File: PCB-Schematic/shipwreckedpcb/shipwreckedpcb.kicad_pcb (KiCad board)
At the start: 4 copper layers, 61.8 x 79.6 mm, 182 parts, among them J1 USB4105, J14 Conn_01x01, J15 Conn_01x01, J16 Conn_01x01, J17 Conn_01x01, J18 Conn_01x01, J19 Conn_01x01, J2 Waveshare 1.54" E-Ink, J20 Conn_01x01, J21 Conn_01x01, J22 Conn_01x01, J23 Conn_01x01, J24 Conn_01x01, J25 Conn_01x01, J26 Conn_01x01, J28 Conn_01x01, J29 Conn_01x01, J3 Conn_01x01, J30 Conn_01x01, J31 Conn_01x01, J32 Conn_01x01, J33 Conn_01x01, J34 Conn_01x01, J35 Conn_01x01, J36 Conn_01x01, J37 Conn_01x01, J38 Conn_01x01, J39 Conn_01x01, J4 Conn_01x01, J40 Conn_01x01, J5 SWD, J6 Conn_01x01, J7 Conn_01x01, J8 B2B Male, J9 B2B Female, Q1 Si1308EDL, SW1 BOOTSEL, SW10 Resistive, SW11 Clicky - THT, SW12 Clicky - SMD, SW13 Clicky - THT, SW14 Clicky - SMD, SW15 Clicky - THT, SW16 Clicky - SMD, SW17 Clicky - THT, SW18 Clicky - SMD, SW19 PWR Switch, SW2 RESET, SW3 Resistive, SW4 Resistive, SW5 Resistive, SW6 Resistive, SW7 Resistive, SW8 Resistive, SW9 Resistive, U1 RP2040, U2 W25Q128JVS, U3 Si4463, U4 TPS61200DRC, U5 AS179-92LF, U6 AMS1117-3.3, U7 PCA9555PW, Y1 ABM8-272-T3, Y2 X322530MOB4SI

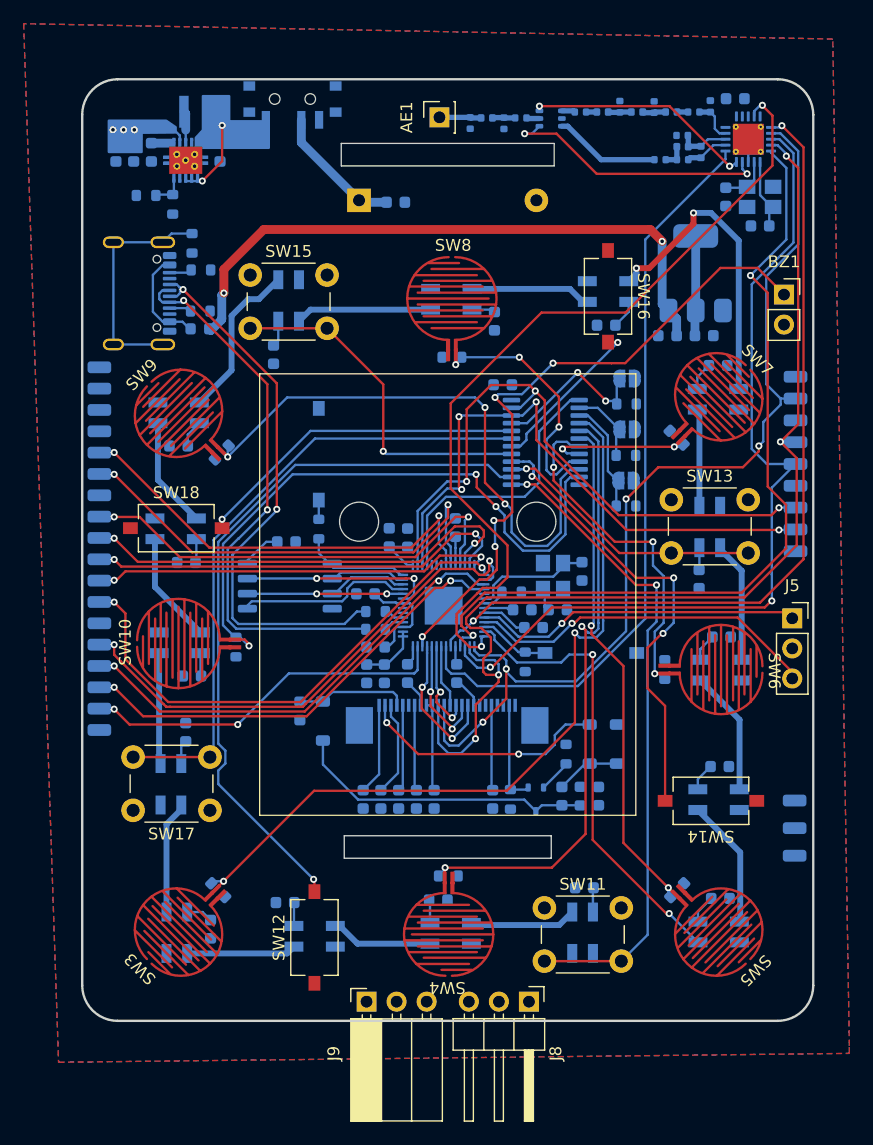
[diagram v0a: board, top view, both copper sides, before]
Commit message: fixed drc errors, added stitching vias
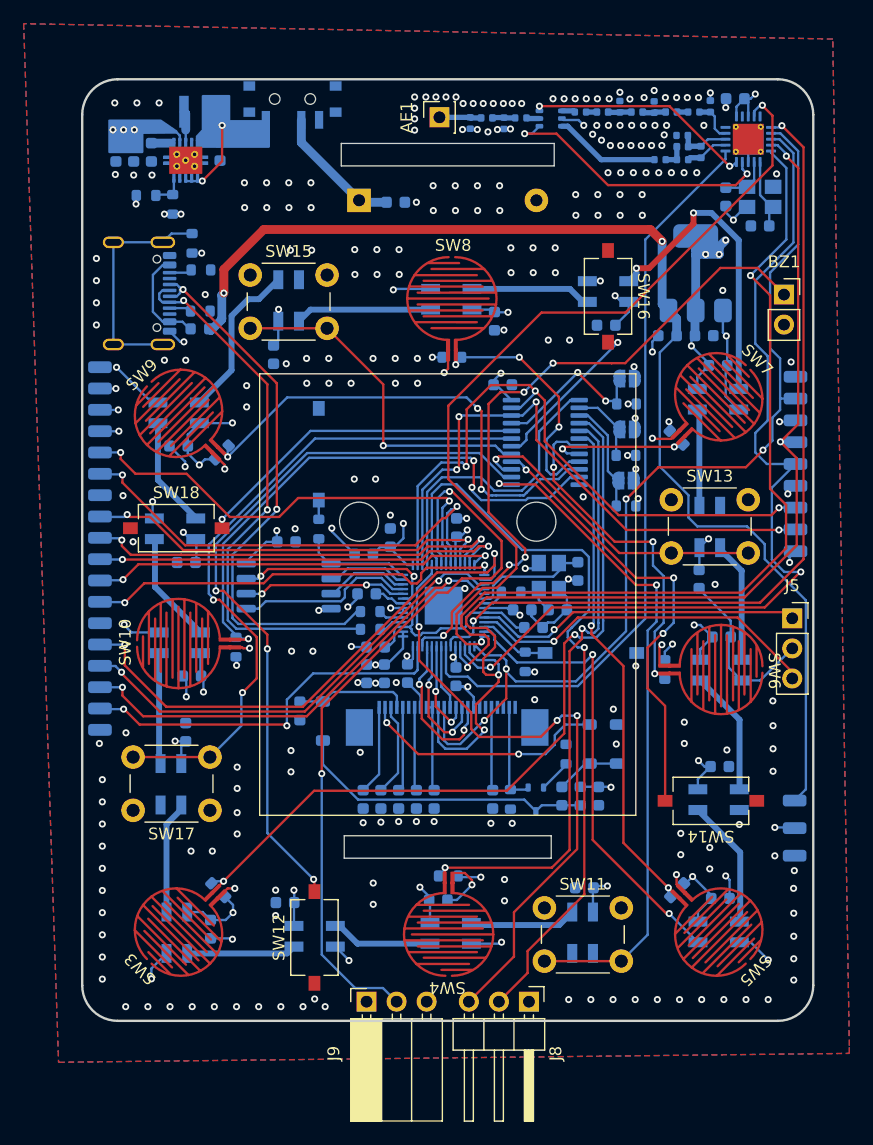
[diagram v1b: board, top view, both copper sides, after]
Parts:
- moved C5 3.96 mm to (139.9, 102.3), turned to 180 degrees
- moved R2 0.45 mm to (140.5, 107.2)
- moved R3 0.45 mm to (140.5, 108.7)
- moved C13 0.35 mm to (158.1, 103.8)
- moved Y1 0.35 mm to (155.6, 104.2)
- moved C8 0.27 mm to (147.8, 112.7)
- moved J2 0.17 mm to (147.0, 116.6)
- moved C6 0.10 mm to (147.8, 100.0)
- moved C1 0.10 mm to (140.2, 105.7)
- moved U2 0.10 mm to (133.6, 105.0)
- moved C4 0.09 mm to (142.2, 100.9)
- moved C53 0.08 mm to (127.8, 68.2)
- moved J24 0.05 mm to (117.7, 111.7)
- moved J6 0.05 mm to (117.7, 90.1)
- moved J14 0.05 mm to (117.7, 93.7)
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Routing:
- net Earth: track 6.95 -> 118.3 mm, vias 0 -> 266
- net +3V3: track 66.2 -> 141.7 mm, vias 3 -> 49
- net /B2B_TX: track 0.00 -> 64.6 mm, vias 0 -> 1
- net /B2B_RX: track 0.00 -> 64.4 mm, vias 0 -> 2
- net /B2B_DCT: track 0.00 -> 54.3 mm, vias 0 -> 3
- net +5V: track 53.1 -> 101.0 mm
- net /GPIO12: track 43.9 -> 35.7 mm
- net +1V1: track 12.8 -> 20.6 mm
- net /BUTT_7: track 49.4 -> 42.2 mm
- net /BUTT_8: track 53.6 -> 48.2 mm
- net /SI_NSEL: track 70.4 -> 75.3 mm
- net /BUTT_15: track 53.7 -> 57.4 mm, vias 0 -> 2
- net /BUTT_11: track 23.0 -> 26.6 mm
- net /SPI_MISO: track 75.0 -> 78.4 mm
- net /GPIO8: track 38.4 -> 35.3 mm
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
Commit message: started sx1262
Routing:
- net Earth: vias 266 -> 268
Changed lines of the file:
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@@
+	)
+	(via
+		(at 143.326388 90.45)
+		(size 0.6)
+		(drill 0.3)
+		(layers "F.Cu" "B.Cu")
+		(free yes)
+		(net 3)
 	)
 	(via
@@
 		(size 0.6)
 		(drill 0.3)
+		(layers "F.Cu" "B.Cu")
+		(free yes)
+		(net 3)
+	)
+	(via
+		(at 145.2 90.45)
+		(size 0.6)
+		(drill 0.3)

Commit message: finished prototype?
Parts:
- removed C26, C27, C28, C29, C30, C31, C32, C33, C34, C35, C36, C37, C38, C39, C40: 100nF, Capacitor_SMD:C_0603_1608Metric
- removed C41: 3.9pF, Capacitor_SMD:C_0402_1005Metric
- removed C42: 5.6pF, Capacitor_SMD:C_0402_1005Metric
- removed C43: 2.7pF, Capacitor_SMD:C_0402_1005Metric
- removed C44, C45, C48: 100pF, Capacitor_SMD:C_0402_1005Metric
- removed C46, C47: 4.3pF, Capacitor_SMD:C_0402_1005Metric
- removed C49: 1pF, Capacitor_SMD:C_0402_1005Metric
- removed C50: 3pF, Capacitor_SMD:C_0402_1005Metric
- removed C58, C59: 12pF, Capacitor_SMD:C_0603_1608Metric
- removed D21, D22, D23, D24, D25, D26, D27, D28, D29, D30, D31, D32, D33, D34, D35, D36: SK6812MINI, LED_SMD:LED_SK6812MINI_PLCC4_3.5x3.5mm_P1.75mm
- removed L2: 100nH, Inductor_SMD:L_0402_1005Metric
- removed L3: 12nH, Inductor_SMD:L_0402_1005Metric
- removed L4, L5: 10nH, Inductor_SMD:L_0402_1005Metric
- removed L6: 8.2nH, Inductor_SMD:L_0402_1005Metric
- removed L7: 22nH, Inductor_SMD:L_0402_1005Metric
- removed L8: 18nH, Inductor_SMD:L_0402_1005Metric
- removed U5: AS179-92LF, Package_TO_SOT_SMD:SOT-363_SC-70-6
- added C57: 47nF, Capacitor_SMD:C_0603_1608Metric, B.Cu at (167.8, 64.8)
- added C62: 47pF, Capacitor_SMD:C_0603_1608Metric, B.Cu at (166.3, 64.3)
- added C63: 100pF, Capacitor_SMD:C_0603_1608Metric, B.Cu at (155.2, 65.5)
- added C64: 1nF, Capacitor_SMD:C_0603_1608Metric, B.Cu at (158.3, 67.9)
- added C65: 100nF, Capacitor_SMD:C_0603_1608Metric, B.Cu at (169.3, 64.5)
- added C66: 100nF, Capacitor_SMD:C_0603_1608Metric, B.Cu at (175.1, 70.5)
- added C67: 470nF, Capacitor_SMD:C_0603_1608Metric, B.Cu at (175.2, 67.0)
- added D5: LED, LED_THT:LED_D5.0mm, B.Cu at (148.3, 65.0)
- added FL1: 0900FM15K0039, RF_Converter:Balun_Johanson_0900FM15K0039, B.Cu at (161.3, 65.2)
- added L10: 47nH, Inductor_SMD:L_0603_1608Metric, B.Cu at (164.1, 64.5)
- added L11: 15uH, Inductor_SMD:L_0805_2012Metric, B.Cu at (176.8, 67.3)
- added R23: 100, Resistor_SMD:R_0603_1608Metric, B.Cu at (161.3, 67.9)
- added U8: SX1262IMLTRT, Package_DFN_QFN:QFN-24-1EP_4x4mm_P0.5mm_EP2.6x2.6mm, B.Cu at (171.7, 68.6)
- C24, C25: value 100nF -> 8pF
- D1: footprint Diode_SMD:D_0603_1608Metric -> Diode_SMD:D_SOD-123F
- U3: value Si4463 -> PE4259; footprint Package_DFN_QFN:QFN-20-1EP_4x4mm_P0.5mm_EP2.6x2.6mm_ThermalVias -> Package_TO_SOT_SMD:SOT-363_SC-70-6
- Y2: value X322530MOB4SI -> 32MHz
- moved C25 67.5 mm to (175.1, 64.0), turned to -90 degrees
- moved U3 14.2 mm to (158.4, 65.5), turned to 180 degrees
- moved Y2 8.09 mm to (172.2, 64.1)
- moved C24 8.03 mm to (167.3, 70.8), turned to 90 degrees
- moved AE1 5.73 mm to (152.1, 64.8)
- moved D1 0.85 mm to (126.8, 83.7)
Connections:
- C24 pad 1: +3V3 -> Earth
- C24 pad 2: Earth -> /SX_XTA
- C25 pad 1: +3V3 -> Earth
- C25 pad 2: Earth -> /SX_XTB
- U1 pad 28: /SI_IO1 -> /SX_DIO1
- U1 pad 32: /SI_NSEL -> /SX_NSS
- U1 pad 34: /SI_NIRQ -> /SX_BUSY
- U1 pad 35: /SI_SDN -> /SX_NRST
- U3 pad 1: /SI_SDN -> Net-(FL1-SW_RFO)
- U3 pad 2: /SI_RXp -> Earth
- U3 pad 3: /SI_RXn -> Net-(FL1-SW_RFI)
- U3 pad 4: /SI_TX -> Net-(U3-CTRL)
- U3 pad 5: unconnected-(U3-NC-Pad5) -> Net-(U3-RFIN)
- Y2 pad 1: /SI_XOUT -> /SX_XTB
- Y2 pad 3: /SI_XIN -> /SX_XTA
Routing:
- net /SI_NSEL: track 75.3 -> 0.00 mm, vias 2 -> 0
- net /SX_NSS: track 0.00 -> 74.2 mm, vias 0 -> 4
- net /SI_NIRQ: track 72.2 -> 0.00 mm, vias 2 -> 0
- net /SI_IO1: track 70.3 -> 0.00 mm, vias 2 -> 0
- net /SX_BUSY: track 0.00 -> 67.9 mm, vias 0 -> 2
- net /SX_NRST: track 0.00 -> 65.2 mm
- net /SI_SDN: track 64.3 -> 0.00 mm
- net /SX_DIO1: track 0.00 -> 63.5 mm, vias 0 -> 2
- net +3V3: track 141.7 -> 81.4 mm, vias 49 -> 41
- net /RGB_DIN: track 38.9 -> 81.3 mm
- net Earth: track 118.3 -> 86.9 mm, vias 268 -> 260
- net Net-(D25-DOUT): track 26.0 -> 0.00 mm, vias 2 -> 0
- net /SI_V1: track 23.7 -> 0.00 mm, vias 2 -> 0
- net /SI_V2: track 19.3 -> 0.00 mm, vias 2 -> 0
- net /SX_XTA: track 0.00 -> 14.4 mm, vias 0 -> 2
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- added copper zone on In1.Cu, net +3V3
- added copper zone on In2.Cu, net Earth
- removed copper zone on In2.Cu, net +3V3
- removed copper zone on In1.Cu, net Earth

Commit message: silkscreen + prod files
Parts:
- added G***: LOGO, LOGO, F.Cu at (171.3, 66.2)
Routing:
- net Earth: vias 260 -> 262
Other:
- board text added: "River Lewis Max Kendall Alex Park Evan Gan"

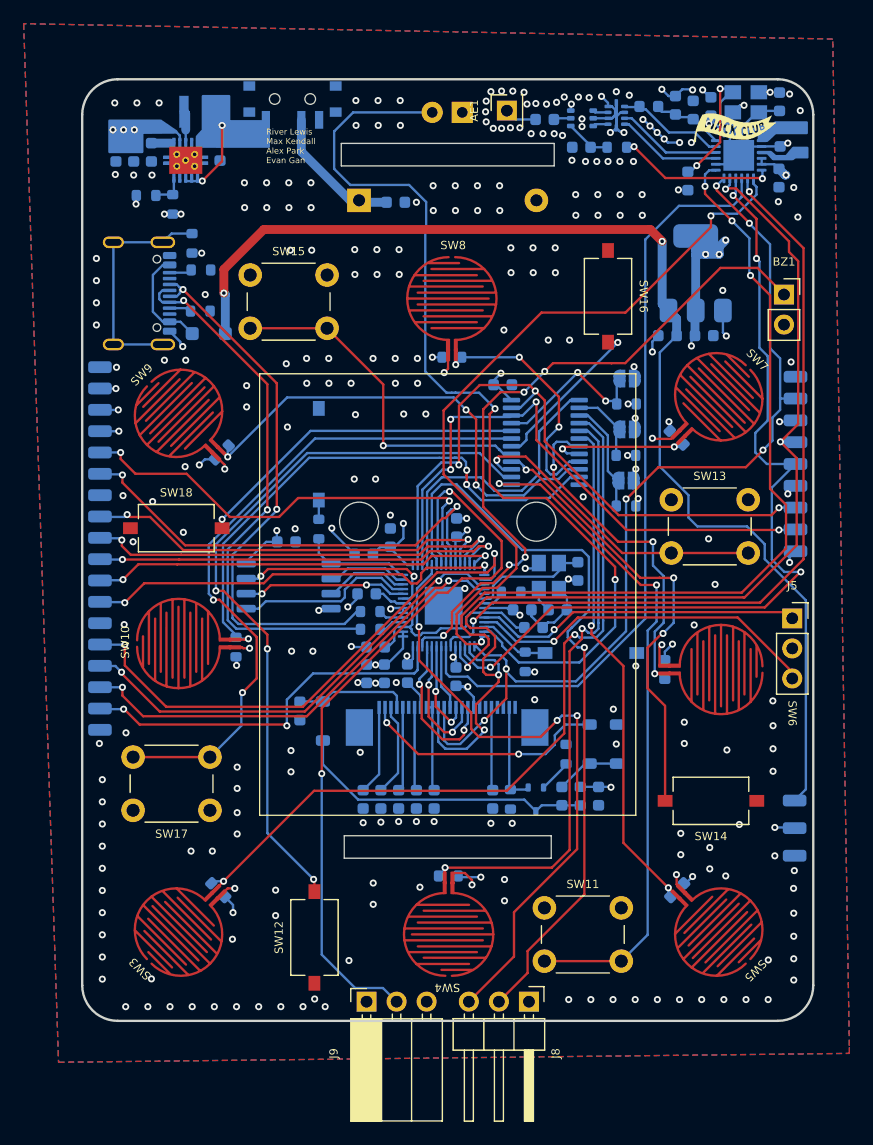
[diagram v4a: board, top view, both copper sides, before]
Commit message: fix dumb stuff
turns out you need to:
- give power :0
- add vgl cap
- not FLIP THE CONNECTOR :heavysob:
- still need to do buttons
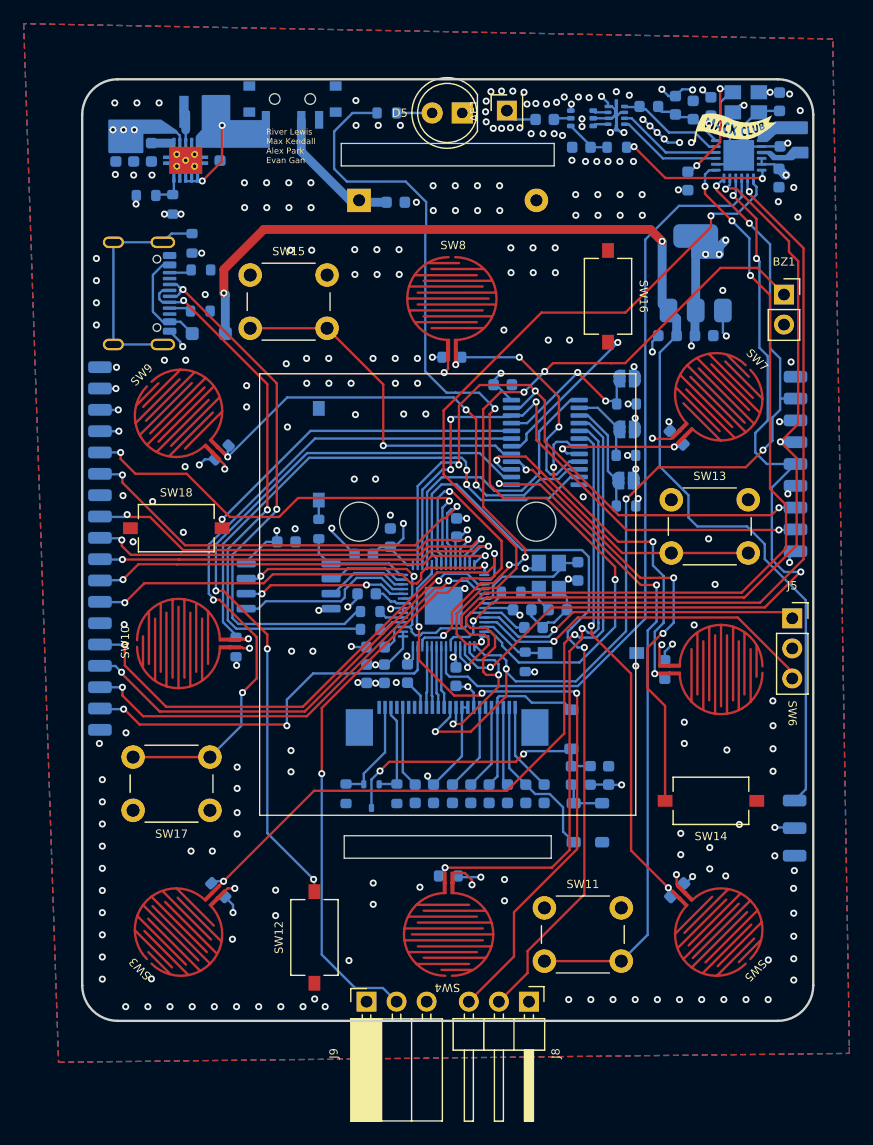
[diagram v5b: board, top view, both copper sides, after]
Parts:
- added C26: 1uF, Capacitor_SMD:C_0603_1608Metric, B.Cu at (153.7, 122.5)
- added R24: 330, Resistor_SMD:R_0603_1608Metric, B.Cu at (141.9, 65.0)
- D5: moved to F.Cu
- moved D4 21.0 mm to (157.5, 117.1)
- moved C23 17.5 mm to (150.6, 122.5)
- moved C20 15.3 mm to (155.2, 122.5)
- moved R8 14.7 mm to (142.8, 122.5), turned to -90 degrees
- moved R9 13.9 mm to (138.5, 122.5)
- moved Q1 13.9 mm to (140.6, 122.8)
- moved C19 10.7 mm to (152.1, 122.5)
- moved D2 6.79 mm to (157.7, 125.0), turned to -90 degrees
- moved D3 6.77 mm to (160.1, 125.0), turned to 90 degrees
- moved C15 6.57 mm to (144.3, 122.5)
- moved C18 6.12 mm to (149.0, 122.5)
- moved C17 3.09 mm to (147.4, 122.5)
- moved C22 1.95 mm to (160.7, 121.0), turned to -90 degrees
- moved L1 1.95 mm to (159.1, 121.0), turned to 90 degrees
- moved C21 1.92 mm to (157.5, 121.0), turned to -90 degrees
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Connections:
- C15 pad 2: Net-(J2-Pin_5) -> Net-(J2-Pin_20)
- C16 pad 2: Net-(J2-Pin_15) -> +3V3
- C17 pad 2: Net-(J2-Pin_18) -> Net-(J2-Pin_7)
- C18 pad 2: Net-(J2-Pin_20) -> Net-(J2-Pin_5)
- C19 pad 2: Net-(J2-Pin_22) -> Net-(J2-Pin_3)
- D5 pad 2: /RGB_DIN -> Net-(D5-A)
- J2 pad 1: unconnected-(J2-Pin_1-Pad1) -> /DISP_VCOM
- J2 pad 10: /DISP_RST -> +3V3
- J2 pad 11: /DISP_DC -> /SPI_MOSI
- J2 pad 12: /DISP_CS -> /SPI_CLK
- J2 pad 13: /SPI_CLK -> /DISP_CS
- J2 pad 14: /SPI_MOSI -> /DISP_DC
- J2 pad 15: Net-(J2-Pin_15) -> /DISP_RST
- J2 pad 16: Net-(J2-Pin_15) -> /DISP_BUSY
- J2 pad 18: Net-(J2-Pin_18) -> unconnected-(J2-Pin_18-Pad18)
- J2 pad 2: /DISP_GDR -> /DISP_PREVGL
- J2 pad 21: /DISP_PREVGH -> unconnected-(J2-Pin_21-Pad21)
- J2 pad 22: Net-(J2-Pin_22) -> /DISP_RESE
- J2 pad 23: /DISP_PREVGL -> /DISP_GDR
- J2 pad 24: /DISP_VCOM -> unconnected-(J2-Pin_24-Pad24)
- J2 pad 3: /DISP_RESE -> Net-(J2-Pin_3)
- J2 pad 4: unconnected-(J2-Pin_4-Pad4) -> /DISP_PREVGH
- J2 pad 7: unconnected-(J2-Pin_7-Pad7) -> Net-(J2-Pin_7)
- J2 pad 9: /DISP_BUSY -> +3V3
- Q1 pad 2: /DISP_RES -> /DISP_RESE
- R8 pad 1: /DISP_RES -> /DISP_RESE
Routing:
- net +3V3: track 81.2 -> 90.2 mm, vias 41 -> 42
- net /DISP_BUSY: track 13.4 -> 5.19 mm, vias 2 -> 0
- net /DISP_RESE: track 0.00 -> 8.19 mm
- net Net-(J2-Pin_22): track 7.85 -> 0.00 mm
- net Net-(J2-Pin_15): track 7.56 -> 0.00 mm
- net Net-(J2-Pin_7): track 0.00 -> 7.48 mm
- net Net-(J2-Pin_18): track 7.06 -> 0.00 mm
- net /DISP_PREVGL: track 21.1 -> 14.4 mm, vias 2 -> 0
- net Net-(J2-Pin_3): track 0.00 -> 6.67 mm
- net /SPI_MOSI: track 93.4 -> 87.4 mm
- net /DISP_RST: track 11.1 -> 5.18 mm, vias 2 -> 0
- net /DISP_PREVGH: track 9.65 -> 14.4 mm
- net /RGB_DIN: track 81.3 -> 76.6 mm
- net /DISP_DC: track 8.40 -> 5.22 mm, vias 2 -> 0
- net Net-(D5-A): track 0.00 -> 3.01 mm
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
